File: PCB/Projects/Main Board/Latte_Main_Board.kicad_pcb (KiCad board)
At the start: 4 copper layers, 114 x 50.5 mm, 120 parts, among them J1 SM02B-SURS-TF_LF__SN_, J2 SM02B-SURS-TF_LF__SN_, J3 Molex 505110-0892, J4 Molex 505110-0592, J5 Molex 505110-0892, J6 Molex 505110-0592, J8 Conn_01x04_Pin, J9 Molex 505110-1792, Q1 MMBT2222A, Q2 MMBT2222A, SW1 SW_Push, SW2 SW_Push, SW3 SW_Push, SW4 SW_Push, SW5 SW_Push, SW6 SW_Push, SW7 SW_Push, SW8 SW_Push, U1 HAL4395, U10 HAL4395, U11 HAL4395, U2 RP2350_80QFN, U3 HAL4395, U4 ST_LSM6, U5 ST_LSM6, U6 HAL4395, U7 HAL4395, U8 HAL4395, U9 HAL4395, Y1 ABM8-272-T3

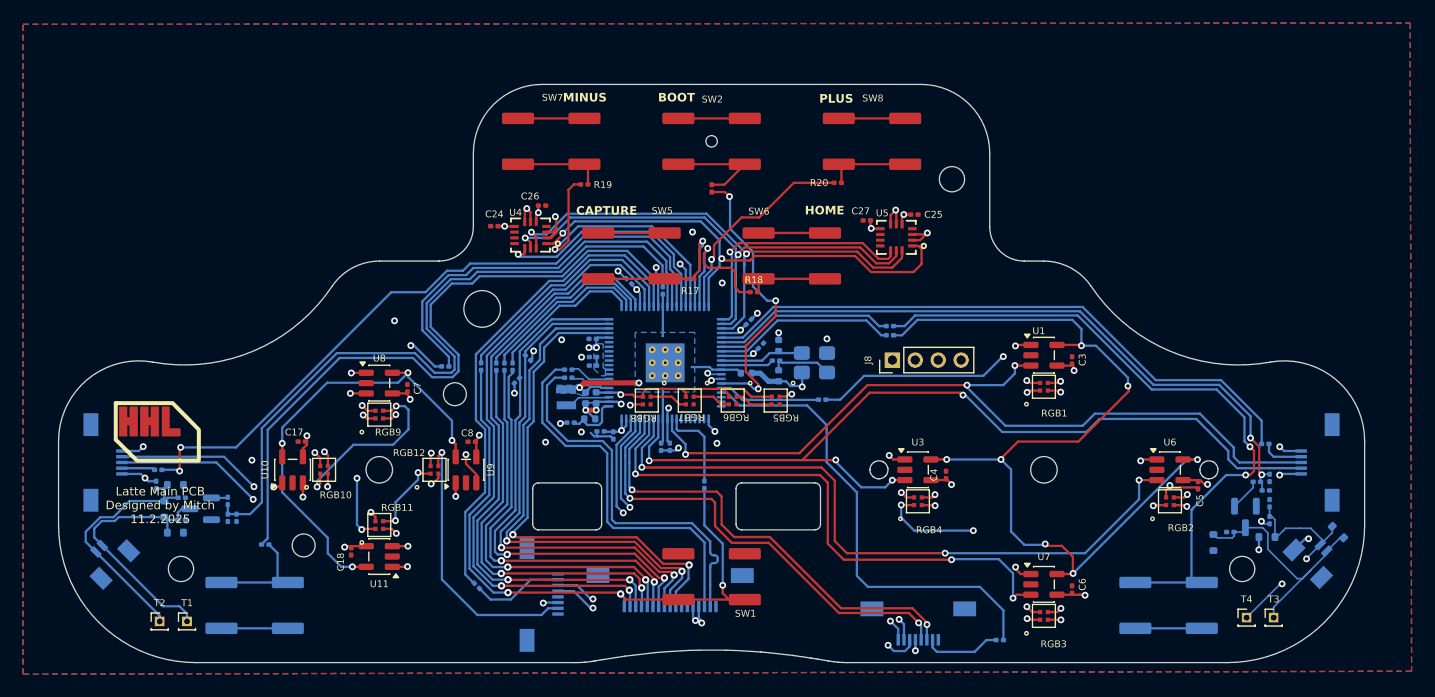
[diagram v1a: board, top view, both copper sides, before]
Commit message: PCB Update
- Missing BOOT switch added
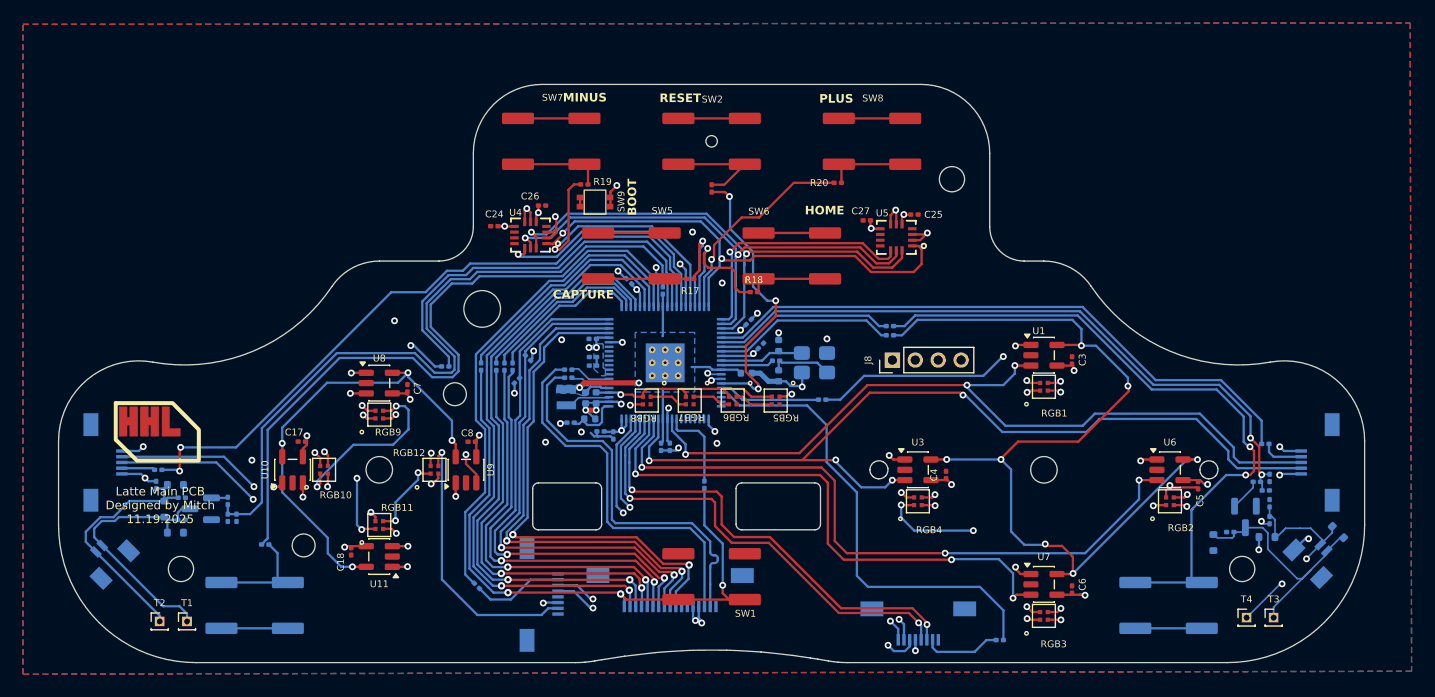
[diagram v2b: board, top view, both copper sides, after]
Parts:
- added SW9: 1TS026A-1000-0550, hhl:1TS026A-1000-0550, F.Cu at (66.0, 32.8)
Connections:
- U2 pad 75: unconnected-(U2-QSPI_SS-Pad75) -> USB_BOOT
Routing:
- net USB_BOOT: track 0.00 -> 17.6 mm, vias 0 -> 2
- net GND: track 122.4 -> 123.3 mm, vias 44 -> 43
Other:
- board text added: "Latte Main PCB Designed by Mitch 11.19.2025"
- board text added: "RESET"
- board text removed: "Latte Main PCB Designed by Mitch 11.2.2025"

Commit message: Silkscreen updates
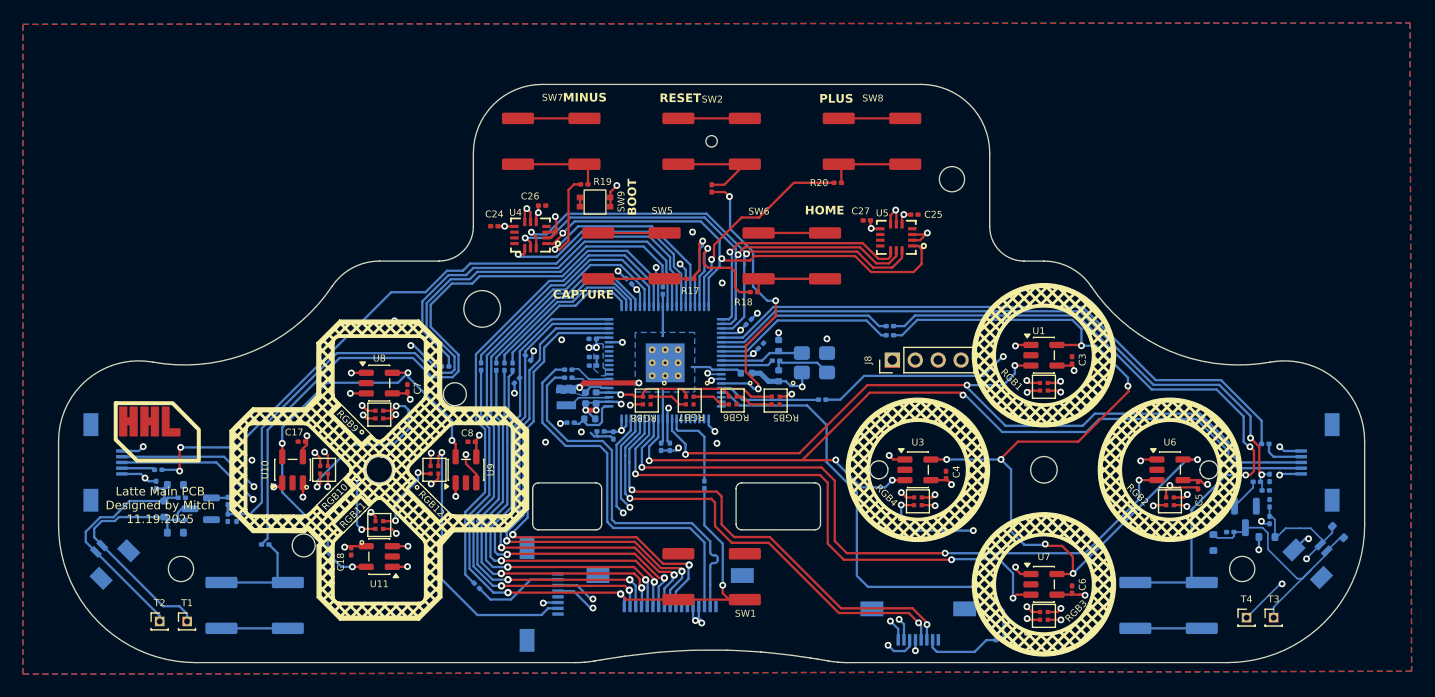
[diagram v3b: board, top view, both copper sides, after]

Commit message: PCB Updates
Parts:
- moved RGB10 0.18 mm to (42.2, 56.2)
- moved RGB9 0.16 mm to (47.2, 51.2)
- moved RGB11 0.16 mm to (47.2, 61.2)
- moved RGB12 0.14 mm to (52.1, 56.2)
- moved RGB3 0.14 mm to (105.2, 68.8)
- moved RGB1 0.14 mm to (105.2, 48.8)
- moved RGB2 0.14 mm to (116.2, 58.8)
- moved RGB4 0.14 mm to (94.2, 58.8)
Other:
- board text added: "Latte Main PCB Designed by Mitch 11.20.2025"
- board text removed: "Latte Main PCB Designed by Mitch 11.19.2025"
